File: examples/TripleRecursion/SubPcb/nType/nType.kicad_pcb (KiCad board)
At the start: 2 copper layers, 8.8 x 0.8 mm, 3 parts, among them Q1 MMBT2222A

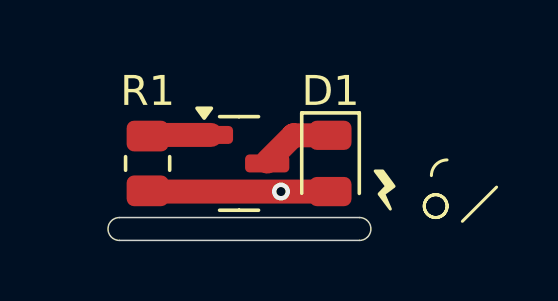
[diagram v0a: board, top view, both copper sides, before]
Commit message: Add Zones to Examples
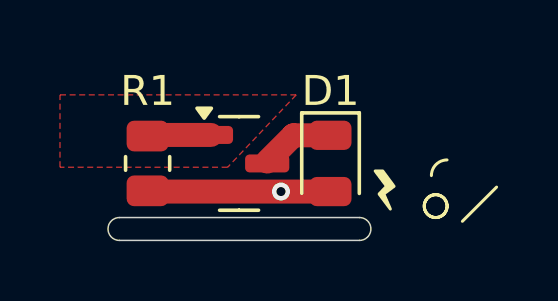
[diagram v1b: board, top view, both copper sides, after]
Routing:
- added copper zone on F.Cu, net /Input
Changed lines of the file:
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@@
 		(net 3)
 	)
+	(zone
+		(net 3)
+		(net_name "/Input")
+		(layer "F.Cu")
+		(hatch edge 0.5)
+		(priority 3)
+		(connect_pads
+			(clearance 0)
+		)
+		(min_thickness 0.25)
+		(filled_areas_thickness no)
+		(fill
+			(thermal_gap 0.5)
+			(thermal_bridge_width 0.5)
+		)
+		(polygon
+			(pts
+				(xy 12.954 15.494) (xy 20.828 15.494) (xy 18.542 17.907) (xy 12.954 17.907)
+			)
+		)
+	)
 )
